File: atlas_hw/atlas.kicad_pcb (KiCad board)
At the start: 4 copper layers, 67 x 70 mm, 169 parts, among them J1 USB_C_Receptacle_USB2.0, J10 PSP_LCD, J2 DEBUG_STM, J3 PSP_TOUCH, J4 DEBUG_NCP, J5 CELL_THERM, J6 LPM027M128B, J7 FLEX_12380-03, J8 Micro_SD_Card_Det, J9 PSP_LCD_BL, Q1 Q_NMOS_DGS, Q4 Q_NMOS_DGS, Q5 Q_NMOS_DGS, SW1 ResetNCP, SW3 ResetSTM, U1 STM32H723VITx, U10 BQ25611D, U11 L96-M33, U12 BGU7007, U13 LSF0108, U14 NPP600SNADJ, U15 TPS61073, U16 PAM2841, U2 S27KL0641DABHV023, U3 MCP1811B, U4 TLV62569DBV, U5 MX25L3233FM2I-08G, U6 LC709203F, U7 BGM220P, U8 MS5637, U9 MC6470, Y1 16M, Y4 32k

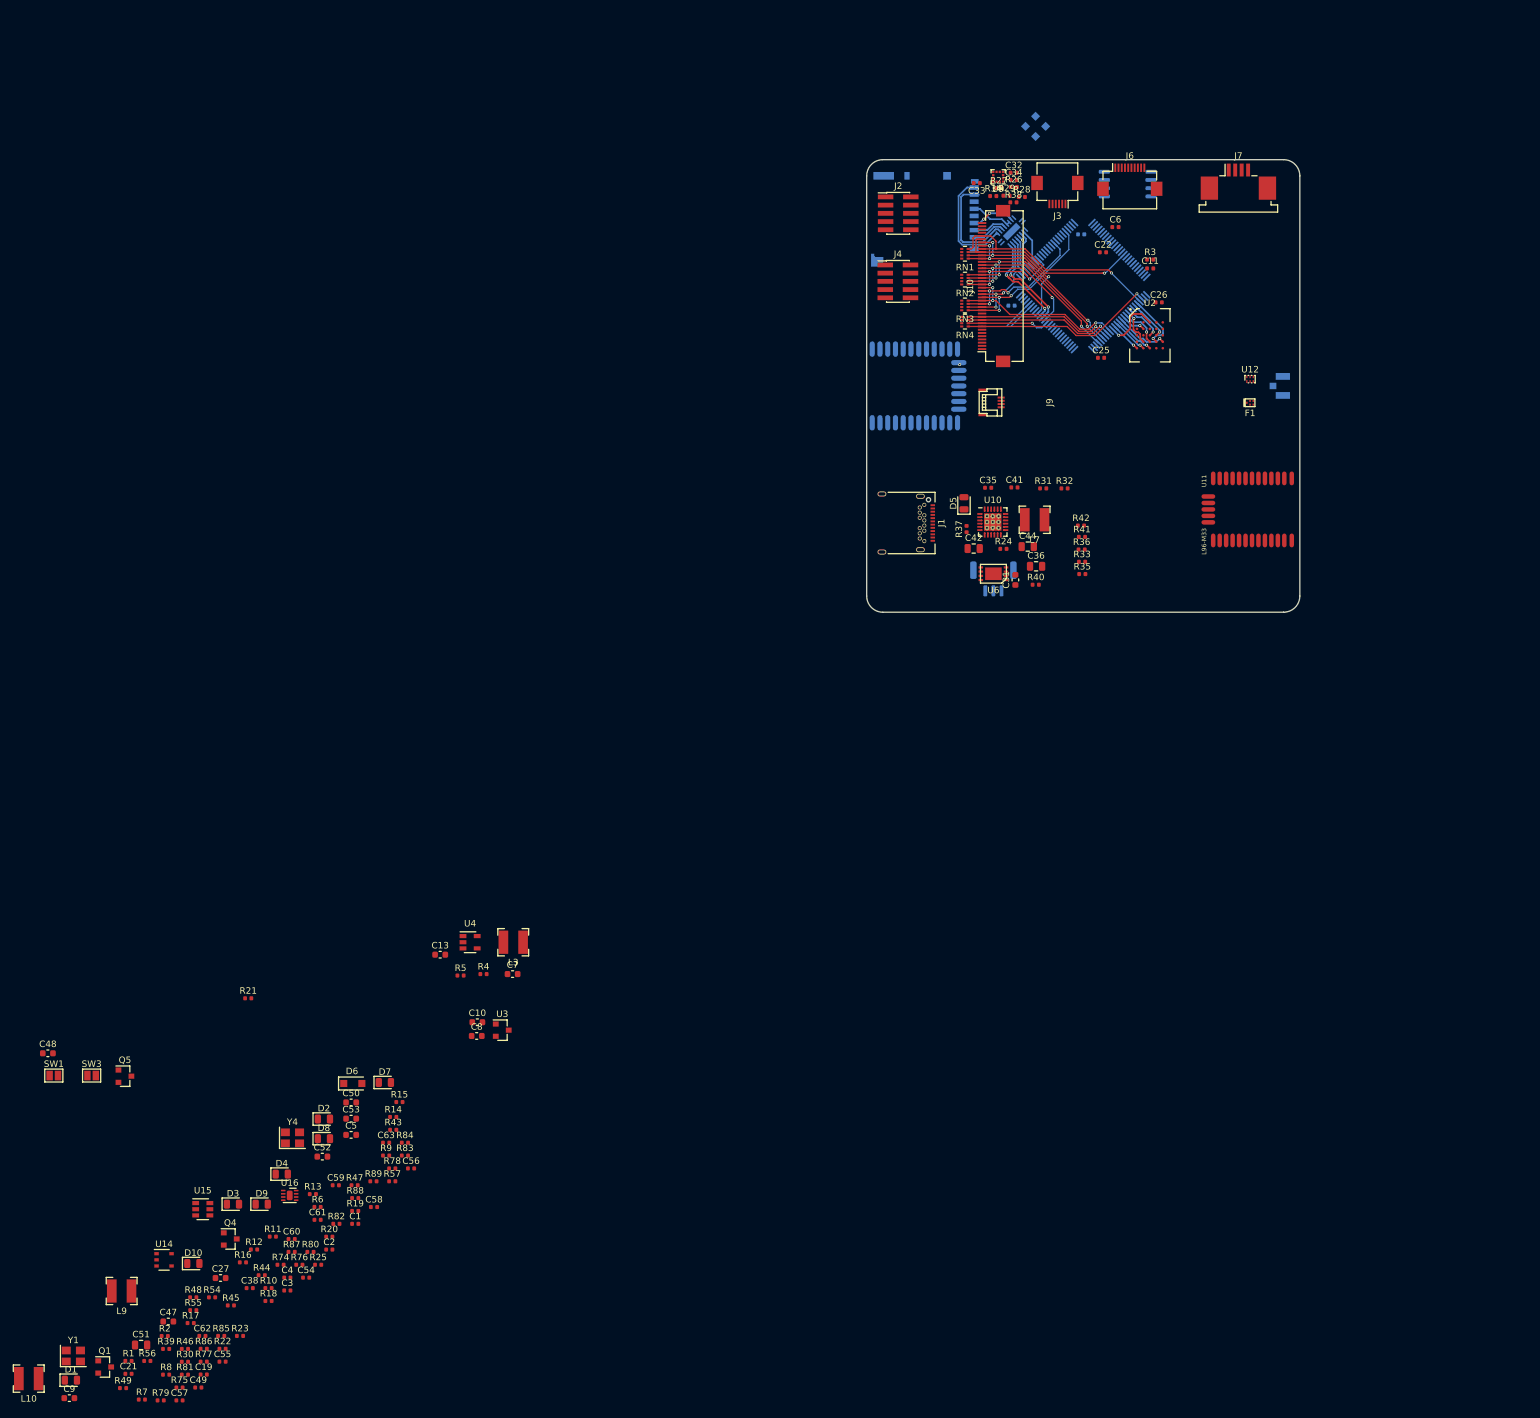
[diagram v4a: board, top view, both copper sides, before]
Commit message: removed bgm220, compacted layout, mounting holes, dss, power supply
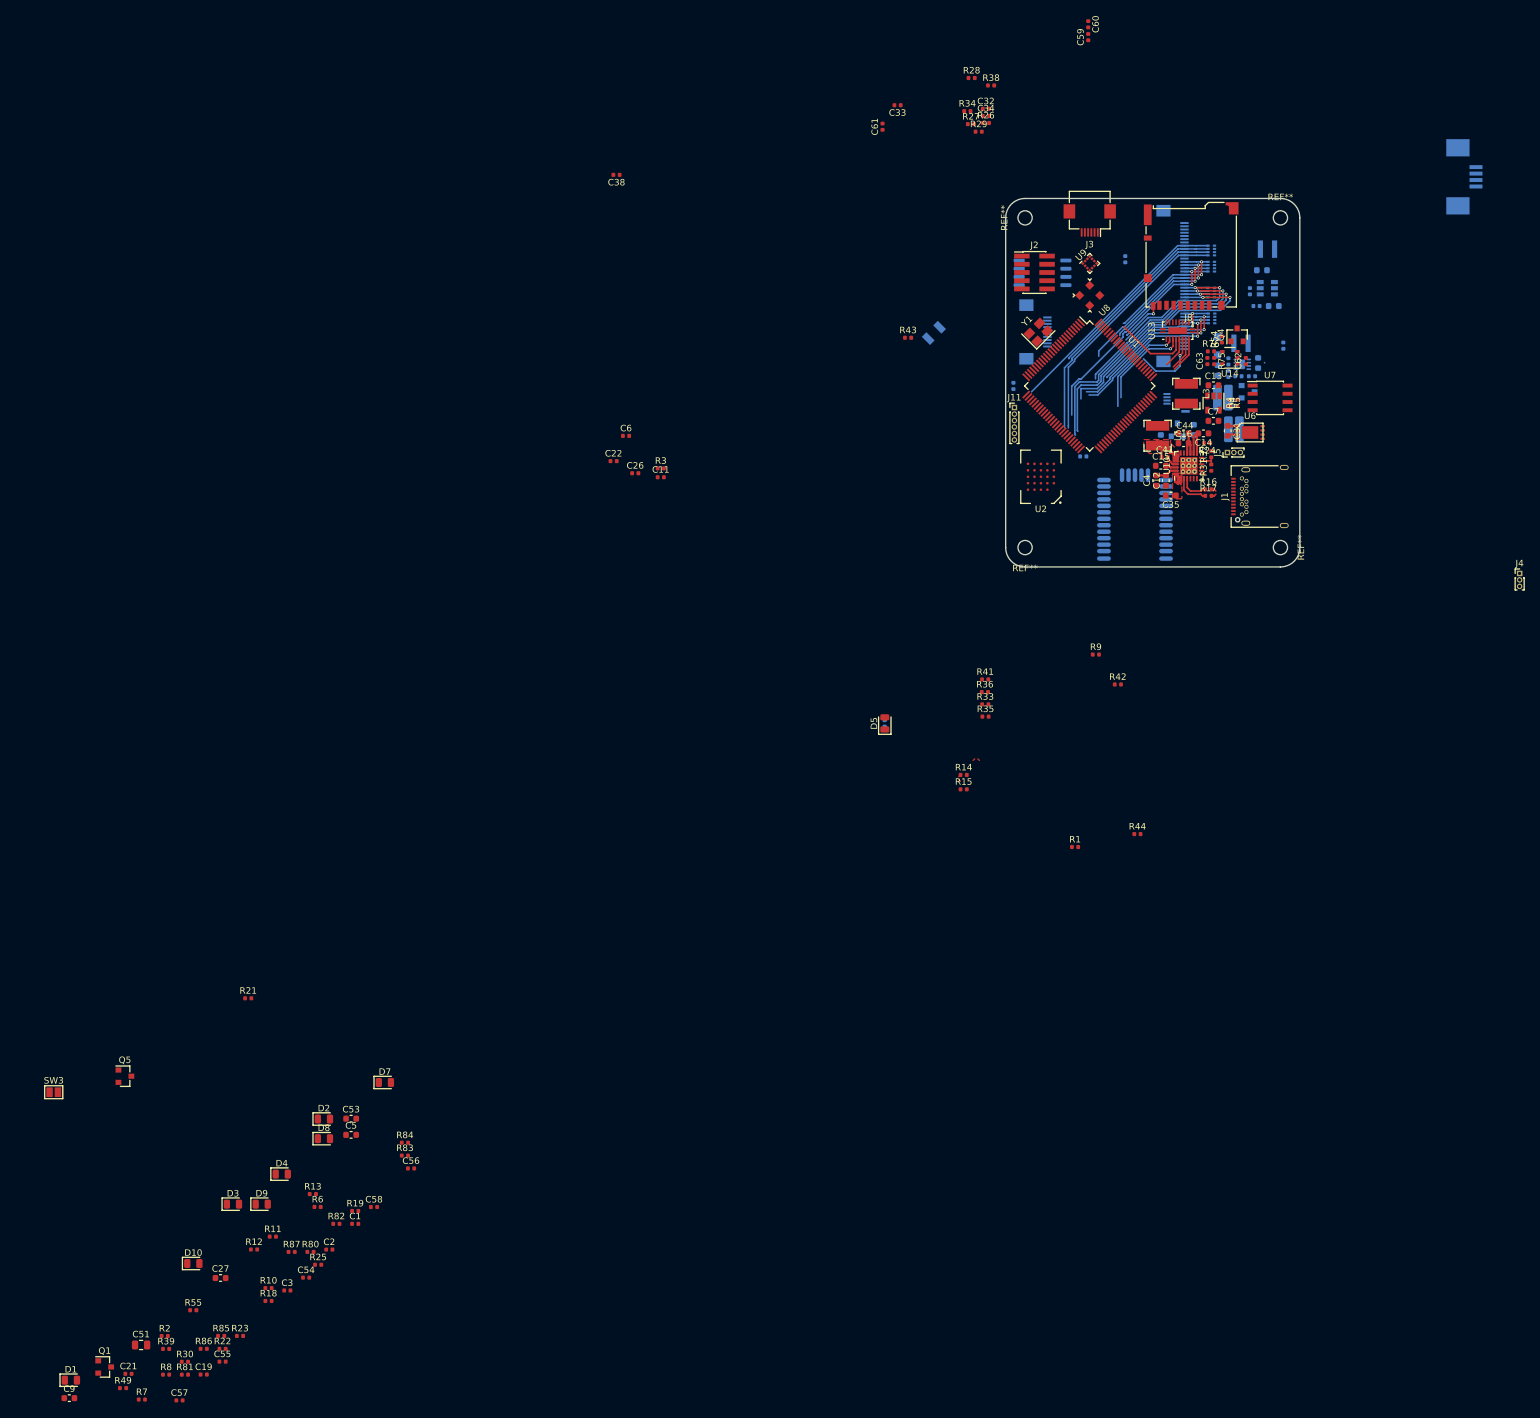
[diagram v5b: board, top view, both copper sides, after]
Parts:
- removed AE1: Antenna_Shield, Connector_Coaxial:U.FL_Hirose_U.FL-R-SMT-1_Vertical
- removed C36, C42: 10u, Capacitor_SMD:C_0805_2012Metric
- removed F1: SF14-1575F5UUC1, Filter:Filter_1411-5_1.4x1.1mm
- removed R45, R48: 100, Resistor_SMD:R_0402_1005Metric
- removed R74, R77: NP, Resistor_SMD:R_0402_1005Metric
- removed R88, R89: 0, Resistor_SMD:R_0402_1005Metric
- removed SW1: ResetNCP, Jumper:SolderJumper-2_P1.3mm_Open_Pad1.0x1.5mm
- removed U12: BGU7007, atlas:6-XSON_1.5x1.0mm_0.5mm
- added C12: 4.7u, Capacitor_SMD:C_0603_1608Metric, F.Cu at (196.3, 128.1)
- added C14: 4.7u, Capacitor_SMD:C_0603_1608Metric, F.Cu at (202.1, 120.8)
- added C15: 4.7u, Capacitor_SMD:C_0603_1608Metric, F.Cu at (195.5, 125.8)
- added C16: 4.7u, Capacitor_SMD:C_0603_1608Metric, F.Cu at (199.0, 122.4)
- added J11: UART3_EXT, Connector_PinHeader_1.00mm:PinHeader_1x06_P1.00mm_Vertical, F.Cu at (172.8, 116.8)
- added Q2: Q_NMOS_DGS, Package_TO_SOT_SMD:SOT-23, B.Cu at (209.0, 114.4)
- added REF**: MountingHole_2.2mm_M2, MountingHole:MountingHole_2.2mm_M2, F.Cu at (174.5, 87.5)
- added REF**: MountingHole_2.2mm_M2, MountingHole:MountingHole_2.2mm_M2, F.Cu at (174.5, 138.5)
- added REF**: MountingHole_2.2mm_M2, MountingHole:MountingHole_2.2mm_M2, F.Cu at (214.0, 138.5)
- added REF**: MountingHole_2.2mm_M2, MountingHole:MountingHole_2.2mm_M2, F.Cu at (214.0, 87.5)
- C10, C25, C47, C48, C49, C50, C52, C8, D6, J10, J6, J7, J9, R37, R46, R47, R56, R57, R78, R79, RN1, RN2, RN3, RN4, U11, U15, U16, U3: moved to B.Cu
- C35: value 0.1u -> 1u; footprint Capacitor_SMD:C_0402_1005Metric -> Capacitor_SMD:C_0603_1608Metric
- C4: value 56p -> 4.7u; footprint Capacitor_SMD:C_0402_1005Metric -> Capacitor_SMD:C_0603_1608Metric
- C44: value 10u -> 4.7u; footprint Capacitor_SMD:C_0805_2012Metric -> Capacitor_SMD:C_0603_1608Metric
- J4: value DEBUG_NCP -> UPDI_DSS; footprint Connector_PinHeader_1.27mm:PinHeader_2x05_P1.27mm_Vertical_SMD -> Connector_PinHeader_1.00mm:PinHeader_1x03_P1.00mm_Vertical
- J5: footprint Connector_JST:JST_GH_SM03B-GHS-TB_1x03-1MP_P1.25mm_Horizontal -> Connector_PinHeader_1.00mm:PinHeader_1x03_P1.00mm_Vertical; moved to F.Cu
- J8, U1, U13, U8: moved to F.Cu
- L10, L9: footprint Inductor_SMD:L_Bourns-SRN4018 -> Inductor_SMD:L_Taiyo-Yuden_MD-3030; moved to B.Cu
- R20: value 10k -> 10; footprint Resistor_SMD:R_0402_1005Metric -> Resistor_SMD:R_0815_2038Metric; moved to B.Cu
- R40: footprint Resistor_SMD:R_0402_1005Metric -> Resistor_SMD:R_0815_2038Metric; moved to B.Cu
- R43: value 0 -> 100k
- R44: value 0 -> 10k
- U7: value BGM220P -> ATtiny402-SS; footprint atlas:BGM220P -> Package_SO:SOIC-8_3.9x4.9mm_P1.27mm; moved to F.Cu
- Y4: footprint Crystal:Crystal_SMD_3225-4Pin_3.2x2.5mm -> Crystal:Crystal_SMD_3215-2Pin_3.2x1.5mm; moved to B.Cu
- moved L10 246.6 mm to (207.9, 106.9), turned to 180 degrees
- moved L9 239.6 mm to (212.0, 92.3)
- moved R56 236.8 mm to (210.3, 101.1)
- moved C47 234.6 mm to (211.1, 95.6), turned to 180 degrees
- moved R46 230.1 mm to (214.4, 107.3), turned to 90 degrees
- moved R79 229.1 mm to (205.9, 111.7), turned to 90 degrees
- moved R75 225.4 mm to (203.8, 109.7), turned to 270 degrees
- moved C60 224.7 mm to (184.3, 57.5), turned to 270 degrees
- moved C49 224.4 mm to (207.5, 112.0)
- moved C62 220.9 mm to (208.7, 109.7), turned to 90 degrees
- moved U15 217.7 mm to (212.0, 98.4), turned to 180 degrees
- moved Y1 217.6 mm to (176.6, 105.2), turned to 45 degrees
- moved U14 216.0 mm to (206.2, 109.2), turned to 180 degrees
- moved C48 215.5 mm to (210.6, 110.0), turned to 90 degrees
- moved R54 215.3 mm to (204.9, 106.3), turned to 90 degrees
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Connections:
- C4 pad 1: Net-(C4-Pad1) -> GND
- C4 pad 2: Net-(C4-Pad2) -> Net-(C12-Pad2)
- C62 pad 1: Net-(C62-Pad1) -> /VCC_MCU_3V3
- C63 pad 1: /VDD_SD_1V8 -> /VDD_SD_IO_3V3_1V8
- J10 pad 1: Net-(J10-Pad1) -> GND
- J10 pad 10: /LTDC_DE -> /LTDC_R5
- J10 pad 11: /LTDC_CK -> /LTDC_R6
- J10 pad 12: GND -> /LTDC_R7
- J10 pad 13: /LTDC_B7 -> /LTDC_G4
- J10 pad 14: /LTDC_B6 -> /LTDC_G5
- J10 pad 15: /LTDC_B5 -> /LTDC_G6
- J10 pad 16: /LTDC_B4 -> /LTDC_G7
- J10 pad 17: /LTDC_B7 -> /LTDC_G4
- J10 pad 18: /LTDC_B6 -> /LTDC_G5
- J10 pad 19: /LTDC_B5 -> /LTDC_G6
- J10 pad 2: Net-(J10-Pad2) -> GND
- J10 pad 20: /LTDC_B4 -> /LTDC_G7
- J10 pad 21: /LTDC_G7 -> /LTDC_B4
- J10 pad 22: /LTDC_G6 -> /LTDC_B5
- J10 pad 23: /LTDC_G5 -> /LTDC_B6
- J10 pad 24: /LTDC_G4 -> /LTDC_B7
- J10 pad 25: /LTDC_G7 -> /LTDC_B4
- J10 pad 26: /LTDC_G6 -> /LTDC_B5
- J10 pad 27: /LTDC_G5 -> /LTDC_B6
- J10 pad 28: /LTDC_G4 -> /LTDC_B7
- J10 pad 29: /LTDC_R7 -> GND
- J10 pad 3: Net-(J10-Pad3) -> Net-(C54-Pad1)
- J10 pad 30: /LTDC_R6 -> /LTDC_CK
- J10 pad 31: /LTDC_R5 -> /LTDC_DE
- J10 pad 32: /LTDC_R4 -> /LTDC_HS
- J10 pad 33: /LTDC_R7 -> /LTDC_VS
- J10 pad 34: /LTDC_R6 -> Net-(J10-Pad34)
- J10 pad 35: /LTDC_R5 -> Net-(C51-Pad1)
- J10 pad 36: /LTDC_R4 -> Net-(C51-Pad1)
- J10 pad 37: Net-(C54-Pad1) -> Net-(J10-Pad37)
- J10 pad 38: Net-(C54-Pad1) -> Net-(J10-Pad38)
- J10 pad 39: GND -> Net-(J10-Pad39)
- J10 pad 4: Net-(J10-Pad4) -> Net-(C54-Pad1)
- J10 pad 40: GND -> Net-(J10-Pad40)
- J10 pad 5: Net-(J10-Pad5) -> /LTDC_R4
- J10 pad 6: Net-(C51-Pad1) -> /LTDC_R5
- J10 pad 7: Net-(J10-Pad7) -> /LTDC_R6
- J10 pad 8: /LTDC_VS -> /LTDC_R7
- J10 pad 9: /LTDC_HS -> /LTDC_R4
- J4 pad 1: /VCC_MCU_3V3 -> GND
- J4 pad 2: /DEBUG_SWDIO_NCP -> /VCC_BACKUP
- J4 pad 3: GND -> /UDPI_DSS
- R1 pad 2: /PWR_EN_O -> /PWR_ACK_DSS
- R20 pad 1: /DEBUG_NRESET_NCP -> GND
- R20 pad 2: /VCC_MCU_3V3 -> Net-(J9-Pad4)
- R39 pad 1: Net-(C4-Pad2) -> Net-(R39-Pad1)
- R43 pad 1: /VCC_MCU_3V3 -> /VDD_SD_IO_3V3_1V8
- R44 pad 1: /VCC_MCU_3V3 -> /VCC_BACKUP
- R44 pad 2: Net-(C62-Pad1) -> /PWR_EN_O
- R47 pad 2: /T3C1_LCD_BL -> /EN_LCD_PWR
- R6 pad 1: /PWR_ACK_I -> /PWR_EN_O
- R75 pad 2: Net-(R74-Pad1) -> /VDD_SD_IO_3V3_1V8
- R82 pad 2: Net-(J10-Pad3) -> Net-(J10-Pad38)
- R83 pad 2: Net-(J10-Pad2) -> Net-(J10-Pad39)
- R84 pad 2: Net-(J10-Pad1) -> Net-(J10-Pad40)
- RN1 pad 1: /LTDC_R7 -> /LTDC_R4
- RN1 pad 2: /LTDC_R6 -> /LTDC_R5
- RN1 pad 3: /LTDC_R5 -> /LTDC_R6
- RN1 pad 4: /LTDC_R4 -> /LTDC_R7
- RN2 pad 1: /LTDC_G7 -> /LTDC_G4
- RN2 pad 2: /LTDC_G6 -> /LTDC_G5
- RN2 pad 3: /LTDC_G5 -> /LTDC_G6
- RN2 pad 4: /LTDC_G4 -> /LTDC_G7
- RN3 pad 1: /LTDC_B7 -> /LTDC_B4
- RN3 pad 2: /LTDC_B6 -> /LTDC_B5
- RN3 pad 3: /LTDC_B5 -> /LTDC_B6
- RN3 pad 4: /LTDC_B4 -> /LTDC_B7
- RN4 pad 1: /LTDC_VS -> /LTDC_CK
- RN4 pad 2: /LTDC_HS -> /LTDC_DE
- RN4 pad 3: /LTDC_DE -> /LTDC_HS
- RN4 pad 4: /LTDC_CK -> /LTDC_VS
- U1 pad 51: /PWR_ACK_NCP -> /PWR_ACK_DSS
- U1 pad 54: /PWR_SW_NCP -> /PWR_SW_DSS
- U1 pad 57: /MC6470_INTA -> /LC709203_INT
- U1 pad 58: /MC6470_INTM -> /BQ25611_INT
- U1 pad 85: /LC709203_INT -> Net-(U1-Pad85)
- U1 pad 87: Net-(U1-Pad87) -> /MC6470_INTM
- U1 pad 88: Net-(U1-Pad88) -> /MC6470_INTA
- U1 pad 97: /BQ25611_INT -> Net-(U1-Pad97)
- U10 pad 23: Net-(C36-Pad1) -> Net-(C12-Pad2)
- U11 pad 17: Net-(C4-Pad2) -> Net-(R39-Pad1)
- U11 pad 28: (no net) -> /GPS_FORCE_ON
- U11 pad 29: /GPS_FORCE_ON -> /GPS_1PPS
- U13 pad 10: Net-(R88-Pad1) -> GND
- U13 pad 11: Net-(R89-Pad1) -> GND
- U13 pad 12: /SD_D1 -> /SD_D2
- U13 pad 13: /SD_D0 -> /SD_D3
- U13 pad 14: /SD_D2 -> /SD_CMD
- U13 pad 15: /SD_D3 -> /SD_CLK
- U13 pad 17: /SD_CLK -> /SD_D0
- U13 pad 18: /SD_CMD -> /SD_D1
- U13 pad 20: /VDD_SD_IO_3V3_1V8 -> Net-(R43-Pad2)
- U13 pad 3: /SDMMC1_CMD -> /SDMMC1_D1
- U13 pad 4: /SDMMC1_CK -> /SDMMC1_D0
- U13 pad 6: /SDMMC1_D3 -> /SDMMC1_CK
- U13 pad 7: /SDMMC1_D2 -> /SDMMC1_CMD
- U13 pad 8: /SDMMC1_D0 -> /SDMMC1_D3
- U13 pad 9: /SDMMC1_D1 -> /SDMMC1_D2
- U14 pad 1: Net-(C62-Pad1) -> /VCC_MCU_3V3
- U14 pad 3: Net-(R43-Pad2) -> /VCC_MCU_3V3
- U14 pad 5: /VDD_SD_1V8 -> /VDD_SD_IO_3V3_1V8
- U16 pad 2: (no net) -> Net-(C48-Pad2)
- U16 pad 3: /T3C1_LCD_BL -> /EN_LCD_PWR
- U7 pad 1: GND -> /VCC_BACKUP
- U7 pad 2: Net-(U7-Pad2) -> /PWR_EN_O
- U7 pad 3: /PWR_SW_IN -> /PWR_SW_DSS
- U7 pad 4: /PWR_EN_O -> /PWR_SW_IN
- U7 pad 6: Net-(U7-Pad6) -> /UDPI_DSS
- U7 pad 7: Net-(U7-Pad7) -> /PWR_ACK_DSS
- U7 pad 8: /DEBUG_SWDCLK_NCP -> GND
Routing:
- net /SD_D1: track 16.9 -> 0.00 mm
- net /SD_D0: track 16.8 -> 0.00 mm
- net /LTDC_G5: track 29.8 -> 46.1 mm, vias 3 -> 2
- net /LTDC_HS: track 12.9 -> 28.8 mm, vias 1 -> 0
- net /LTDC_DE: track 23.4 -> 39.0 mm, vias 1 -> 0
- net /LTDC_CK: track 23.1 -> 38.3 mm, vias 1 -> 0
- net /LTDC_G4: track 30.5 -> 44.7 mm, vias 3 -> 2
- net /LTDC_B6: track 14.9 -> 26.5 mm, vias 3 -> 2
- net /LTDC_G6: track 22.8 -> 34.0 mm, vias 3 -> 2
- net Net-(C41-Pad1): track 0.00 -> 11.0 mm
- net /SDMMC1_CKIN: track 0.82 -> 11.7 mm, vias 1 -> 0
- net /OCTOSPIM_P1_NCS: track 9.14 -> 0.00 mm, vias 1 -> 0
- net /LTDC_R4: track 35.4 -> 26.5 mm, vias 1 -> 2
- net /OCTOSPIM_P1_IO3: track 8.81 -> 0.00 mm, vias 1 -> 0
- net /LTDC_G7: track 17.5 -> 26.2 mm, vias 3 -> 2
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- added copper zone on F.Cu, net /USB_PORT_VBUS
- added copper zone on F.Cu, net Net-(C41-Pad1)
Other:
- board size 67 x 70 mm -> 45.5 x 57 mm

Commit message: further layout shrink, button board
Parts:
- removed the REF** at (214.0, 138.5)
- removed the REF** at (214.0, 87.5)
- added C17: 0.1u, Capacitor_SMD:C_0402_1005Metric, B.Cu at (83.7, 46.2)
- added C18: 0.1u, Capacitor_SMD:C_0402_1005Metric, F.Cu at (202.2, 30.7)
- added J12: IO_EXT, Connector_FFC-FPC:Hirose_FH12-10S-0.5SH_1x10-1MP_P0.50mm_Horizontal, B.Cu at (79.4, 49.4)
- added J13: IO_MAIN, Connector_FFC-FPC:Hirose_FH12-10S-0.5SH_1x10-1MP_P0.50mm_Horizontal, B.Cu at (178.4, 106.8)
- added R45: 100k, Resistor_SMD:R_0805_2012Metric, B.Cu at (110.8, 50.0)
- added R48: 100k, Resistor_SMD:R_0805_2012Metric, B.Cu at (126.4, 49.9)
- added R50: 100k, Resistor_SMD:R_0805_2012Metric, B.Cu at (129.4, 45.5)
- added REF**: MountingHole_2.2mm_M2, MountingHole:MountingHole_2.2mm_M2, F.Cu at (98.2, 53.9)
- added REF**: MountingHole_2.2mm_M2, MountingHole:MountingHole_2.2mm_M2, F.Cu at (134.2, 53.9)
- added REF**: MountingHole_2.2mm_M2, MountingHole:MountingHole_2.2mm_M2, F.Cu at (214.0, 138.8)
- added REF**: MountingHole_2.2mm_M2, MountingHole:MountingHole_2.2mm_M2, F.Cu at (214.0, 87.8)
- added SW1: BTN_L_EXT, Button_Switch_SMD:SW_SPST_B3S-1000, B.Cu at (89.6, 47.6)
- added SW2: BTN_0_EXT, Button_Switch_SMD:SW_SPST_B3S-1000, B.Cu at (104.1, 47.6)
- added SW4: BTN_R_EXT, Button_Switch_SMD:SW_SPST_B3S-1000, B.Cu at (119.6, 47.6)
- added SW5: BTN_PWR_EXT, Button_Switch_SMD:SW_SPST_B3U-1000P, B.Cu at (132.8, 47.8)
- C13, C7: value 1u -> 10u; footprint Capacitor_SMD:C_0603_1608Metric -> Capacitor_SMD:C_0805_2012Metric
- C47, C50, L9, R56, R57, U15: moved to F.Cu
- D10, D8, D9, Q1, Q5, R42, R85: moved to B.Cu
- D6: footprint Diode_SMD:D_SOD-123F -> Diode_SMD:D_SOD-110
- J7: footprint Connector_FFC-FPC:TE_84952-4_1x04-1MP_P1.0mm_Horizontal -> Connector_PinHeader_1.00mm:PinHeader_1x02_P1.00mm_Vertical
- R11, R18, R19: footprint Resistor_SMD:R_0402_1005Metric -> Resistor_SMD:R_0805_2012Metric; moved to B.Cu
- R20: footprint Resistor_SMD:R_0815_2038Metric -> Resistor_SMD:R_0603_1608Metric
- R40: value 0 -> 100k; footprint Resistor_SMD:R_0815_2038Metric -> Resistor_SMD:R_0805_2012Metric
- R46: footprint Resistor_SMD:R_0402_1005Metric -> Resistor_SMD:R_0612_1632Metric
- moved R85 223.7 mm to (226.9, 123.3), turned to 90 degrees
- moved Q1 220.6 mm to (198.4, 120.3), turned to 180 degrees
- moved D10 219.1 mm to (119.6, 42.9)
- moved R49 218.5 mm to (196.2, 121.1), turned to 270 degrees
- moved R18 218.0 mm to (107.5, 42.9), turned to 180 degrees
- moved Q5 212.7 mm to (224.6, 123.3), turned to 180 degrees
- moved R7 211.7 mm to (204.2, 139.4), turned to 90 degrees
- moved R8 208.9 mm to (207.4, 139.4), turned to 90 degrees
- moved D1 205.2 mm to (187.4, 139.4), turned to 90 degrees
- moved R11 205.2 mm to (93.1, 42.9), turned to 180 degrees
- moved R19 205.0 mm to (123.1, 42.9), turned to 180 degrees
- moved D9 202.8 mm to (104.1, 42.9)
- moved SW3 200.0 mm to (183.4, 101.7)
- moved R25 192.0 mm to (185.4, 99.8)
- moved D8 188.5 mm to (89.6, 42.9)
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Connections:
- D10 pad 1: Net-(D10-Pad1) -> GND
- D10 pad 2: /STM_STATUS_R -> Net-(D10-Pad2)
- D8 pad 1: Net-(D8-Pad1) -> GND
- D8 pad 2: /STM_STATUS_L -> Net-(D8-Pad2)
- D9 pad 1: Net-(D9-Pad1) -> GND
- D9 pad 2: /STM_STATUS_0 -> Net-(D9-Pad2)
- J5 pad 3: /CELL_NEG -> GND
- R11 pad 1: Net-(D8-Pad1) -> /STM_STATUS_L_EXT
- R11 pad 2: GND -> Net-(D8-Pad2)
- R18 pad 1: Net-(D9-Pad1) -> /STM_STATUS_0_EXT
- R18 pad 2: GND -> Net-(D9-Pad2)
- R19 pad 1: Net-(D10-Pad1) -> /STM_STATUS_R_EXT
- R19 pad 2: GND -> Net-(D10-Pad2)
- R40 pad 1: GND -> /VCC_3V3_EXT
- R40 pad 2: /CELL_NEG -> /SW_L_EXT
- U1 pad 97: Net-(U1-Pad97) -> /STM_STATUS_B
- U13 pad 1: GND -> /VDD_SD_IO_3V3_1V8
- U13 pad 10: GND -> /SDMMC1_D1
- U13 pad 11: GND -> /SD_D1
- U13 pad 12: /SD_D2 -> /SD_D0
- U13 pad 13: /SD_D3 -> /SD_CLK
- U13 pad 14: /SD_CMD -> /SD_CLK
- U13 pad 15: /SD_CLK -> /SD_CMD
- U13 pad 16: /SD_CLK -> /SD_D3
- U13 pad 17: /SD_D0 -> /SD_D2
- U13 pad 18: /SD_D1 -> GND
- U13 pad 19: /VDD_SD_IO_3V3_1V8 -> GND
- U13 pad 2: /VCC_MCU_3V3 -> Net-(R43-Pad2)
- U13 pad 20: Net-(R43-Pad2) -> /VCC_MCU_3V3
- U13 pad 21: GND -> /VDD_SD_IO_3V3_1V8
- U13 pad 3: /SDMMC1_D1 -> GND
- U13 pad 4: /SDMMC1_D0 -> /SDMMC1_D2
- U13 pad 5: /SDMMC1_CKIN -> /SDMMC1_D3
- U13 pad 6: /SDMMC1_CK -> /SDMMC1_CMD
- U13 pad 7: /SDMMC1_CMD -> /SDMMC1_CK
- U13 pad 8: /SDMMC1_D3 -> /SDMMC1_CKIN
- U13 pad 9: /SDMMC1_D2 -> /SDMMC1_D0
- U7 pad 4: /PWR_SW_IN -> /SW_PWR
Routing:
- net GND: track 2.09 -> 34.9 mm, vias 0 -> 1
- net /SDMMC1_D1: track 15.3 -> 0.00 mm, vias 1 -> 0
- net Net-(C52-Pad2): track 0.00 -> 12.9 mm
- net /OCTOSPIM_P1_IO2: track 0.00 -> 11.9 mm, vias 0 -> 2
- net /OCTOSPIM_P1_NCS: track 0.00 -> 11.4 mm, vias 0 -> 2
- net /OCTOSPIM_P1_CLK: track 0.00 -> 11.3 mm, vias 0 -> 2
- net /OCTOSPIM_P1_DQS: track 0.00 -> 11.1 mm, vias 0 -> 2
- net /OCTOSPIM_P1_IO3: track 0.00 -> 11.1 mm, vias 0 -> 2
- net /OCTOSPIM_P1_IO1: track 0.00 -> 10.2 mm, vias 0 -> 2
- net /OCTOSPIM_P1_IO4: track 0.00 -> 9.77 mm, vias 0 -> 2
- net /OCTOSPIM_P1_IO0: track 0.00 -> 9.31 mm, vias 0 -> 2
- net /SDMMC1_D2: track 5.60 -> 14.4 mm, vias 0 -> 1
- net /SDMMC1_D0: track 14.4 -> 5.60 mm, vias 1 -> 0
- net Net-(J9-Pad4): track 0.00 -> 7.68 mm
- net /VCC_MCU_3V3: track 0.00 -> 7.54 mm
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- removed copper zone on F.Cu, net /USB_PORT_VBUS
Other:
- board size 45.5 x 57 mm -> 140.3 x 99.9 mm
